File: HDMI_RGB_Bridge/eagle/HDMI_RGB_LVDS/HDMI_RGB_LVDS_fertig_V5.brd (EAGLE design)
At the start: 90 x 60 mm, 92 parts, among them CON1 KLDX-0202-A-LT, CON2 FCI-10029449-111RLF, CON3 XF2M-4015-1A, CON4 FCI-10033526-N3212LF, CON5 MOLEX-53261-0671, CON6 FI-X30SSLA-HF, IC2 WPMDL1300331BD, IC4 AT24C01C-SSHM-B, IC5 TFP401APZP, IC6 ATMEGA48A-AU, IC7 FT232RL, IC8 SN75LVDS83BDGGR, Q1 ATS073ASM-1, T1 IRF9530NSTRRPBF, T2 IRLML2502TRPBF

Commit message: schematic and layout adapted
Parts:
- removed C5: 10u, SchlegelAr_Master:C_POL_4X4MM
- removed LED4: (no value), SchlegelAr_Master:LED0402
- added LED1: (no value), SchlegelAr_Master:LED0402
- added R14: 22R, SchlegelAr_Master:R0402
- C16, C18, C20: value 0.1u -> 100n
- IC6: value ATMEGA48A-AU -> ATMEGA88PA
- R19: value 10k -> 5k
- T1: value IRF9530NSTRRPBF -> IRLML5203TRPBF; device SchlegelAr_Master:D2PAK -> SchlegelAr_Master:SOT23
- moved C1 49.1 mm to (43.2, 53.4)
- moved R25 35.1 mm to (63.4, 19.6), turned to 0 degrees
- moved R15 34.7 mm to (29.1, 22.6), turned to 90 degrees
- moved CON1 33.4 mm to (59.5, 32.4), turned to 180 degrees
- moved JP3 33.3 mm to (31.1, 23.1), turned to 180 degrees
- moved LED2 30.9 mm to (65.7, 21.2), turned to 0 degrees
- moved R27 30.6 mm to (63.4, 21.2), turned to 0 degrees
- moved T1 30.1 mm to (62.9, 39.8)
- moved R20 25.7 mm to (39.8, 55.6)
- moved T2 25.6 mm to (36.2, 54.6), turned to 0 degrees
- moved R1 24.9 mm to (66.0, 40.9), turned to 180 degrees
- moved IC2 20.8 mm to (59.6, 51.0)
- moved C2 17.6 mm to (66.0, 48.6), turned to 270 degrees
- moved JP2 10.1 mm to (58.0, 25.8), turned to 90 degrees
- moved R13 9.91 mm to (13.4, 5.00), flipped to the bottom
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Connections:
- new net N$1: IC6.13, R14.1
- net +12V: now also LED2.C, T1.2; no longer LED4.C, T1.3
- net +3V3: now also LED1.C; no longer LED2.C
- net AVR_PWM: now also R14.2; no longer IC6.13
- net N$2: now also T1.3; no longer T1.2
- net N$6: now also LED1.A; no longer LED2.A
- net N$8: now also LED2.A; no longer LED4.A
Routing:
- net +12V: track 135.6 -> 164.4 mm, vias 3 -> 12
- net RGB_DISP: track 50.7 -> 21.8 mm, vias 2 -> 0
- net N$37: track 36.5 -> 8.13 mm
- net RGB_PWM_EN: track 62.5 -> 39.7 mm, vias 2 -> 1
- net +3V3: track 77.5 -> 67.5 mm, vias 28 -> 36
- net N$2: track 14.9 -> 6.70 mm
- net +5V_USB: track 14.0 -> 20.8 mm
- net GND: track 146.6 -> 153.3 mm, vias 97 -> 103
- net HDMI_PIXS: track 13.6 -> 7.08 mm
- net N$1: track 0.00 -> 5.61 mm
- net LVDS_REVSCAN: track 40.9 -> 43.7 mm
- net AVR_PWM: track 5.25 -> 2.94 mm
- net INT_RGB_EVEN_B7: track 16.0 -> 17.5 mm
- net HDMI_OCK_INV: track 7.03 -> 5.66 mm
- net LVDS_PWM: track 26.2 -> 27.5 mm
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- added copper zone on layer 1, net +12V
- removed copper zone on layer 1, net +5V
- removed copper zone on layer 16, net +5V
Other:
- board size 90 x 60 mm -> 70 x 60 mm
- board text added: "02.04.2014"
- board text removed: "01.04.2014"
- board text removed: "TODO: vias verschieben, platine verkleiner, luftlinien killen"

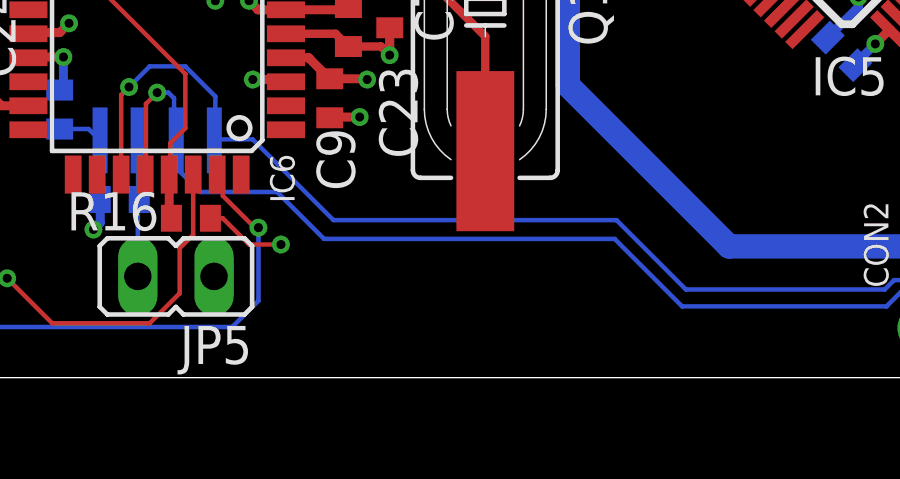
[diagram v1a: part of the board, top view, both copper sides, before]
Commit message: writing and reading to eeprom works - checksum needs to be fixed
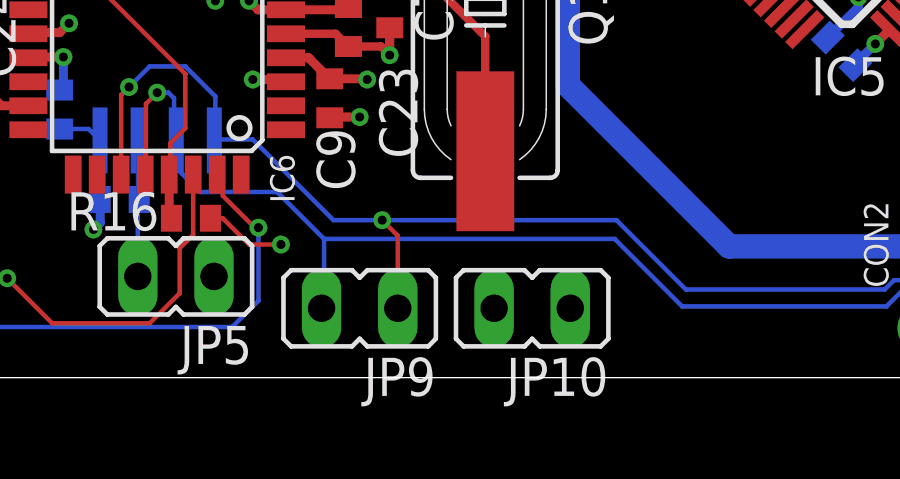
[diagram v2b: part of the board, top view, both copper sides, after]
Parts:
- added JP10, JP9: JUMPER2, SchlegelAr_Master:JUMPER2_THROUGHHOLE
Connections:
- net +5V: now also JP10.2
- net EDID_SCL: now also JP9.2
- net EDID_SDA: now also JP9.1
- net GND: now also JP10.1
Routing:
- net EDID_SDA: track 50.6 -> 53.8 mm, vias 2 -> 3
- net EDID_SCL: track 50.9 -> 53.3 mm
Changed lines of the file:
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@@
 <layers>
 <layer number="1" name="Top" color="4" fill="1" visible="yes" active="yes"/>
-<layer number="2" name="Route2" color="1" fill="3" visible="no" active="yes"/>
+<layer number="2" name="Route2" color="1" fill="3" visible="yes" active="yes"/>
 <layer number="3" name="Route3" color="4" fill="3" visible="no" active="no"/>
 <layer number="14" name="Route14" color="1" fill="6" visible="no" active="no"/>
-<layer number="15" name="Route15" color="4" fill="6" visible="no" active="yes"/>
+<layer number="15" name="Route15" color="4" fill="6" visible="yes" active="yes"/>
 <layer number="16" name="Bottom" color="1" fill="1" visible="yes" active="yes"/>
 <layer number="17" name="Pads" color="2" fill="1" visible="yes" active="yes"/>
@@
 <layer number="19" name="Unrouted" color="6" fill="1" visible="yes" active="yes"/>
 <layer number="20" name="Dimension" color="15" fill="1" visible="yes" active="yes"/>
-<layer number="21" name="tPlace" color="7" fill="1" visible="no" active="yes"/>
+<layer number="21" name="tPlace" color="7" fill="1" visible="yes" active="yes"/>
 <layer number="22" name="bPlace" color="7" fill="1" visible="no" active="yes"/>
-<layer number="23" name="tOrigins" color="15" fill="1" visible="no" active="yes"/>
+<layer number="23" name="tOrigins" color="15" fill="1" visible="yes" active="yes"/>
 <layer number="24" name="bOrigins" color="15" fill="1" visible="no" active="yes"/>
 <layer number="25" name="tNames" color="7" fill="1" visible="no" active="yes"/>
@@
 <attribute name="VALUE" x="24.865" y="13.7825" size="1.27" layer="27"/>
 </element>
+<element name="JP9" library="SchlegelAr_Master" package="JUMPER2_THROUGHHOLE" value="JUMPER2" x="27.5" y="2.3125" rot="R90"/>
+<element name="JP10" library="SchlegelAr_Master" package="JUMPER2_THROUGHHOLE" value="JUMPER2" x="33.25" y="2.3125" rot="R90"/>
 </elements>
 <signals>
@@
 <via x="28.1875" y="51.25" extent="1-16" drill="0.3"/>
 <via x="28.875" y="50.5625" extent="1-16" drill="0.3"/>
+<contactref element="JP10" pad="1"/>
 </signal>
 <signal name="+3V3">
@@
 <wire x1="14.0875" y1="5" x2="15" y2="5" width="0.3" layer="16"/>
 <via x="15" y="5" extent="1-16" drill="0.3"/>
+<contactref element="JP10" pad="2"/>
 </signal>
 <signal name="N$2">
@@
 <wire x1="54.8125" y1="3.375" x2="56.875" y2="3.375" width="0.15" layer="16"/>
 <wire x1="56.875" y1="4.6875" x2="56.875" y2="3.375" width="0.15" layer="1"/>
-<wire x1="26.625" y1="5.25" x2="36.0625" y2="5.25" width="0.15" layer="16"/>
+<wire x1="26.625" y1="5.25" x2="28.0625" y2="5.25" width="0.15" layer="16"/>
+<wire x1="28.25" y1="5.25" x2="36.0625" y2="5.25" width="0.15" layer="16"/>
 <wire x1="36.0625" y1="5.25" x2="38.375" y2="2.9375" width="0.15" layer="16"/>
 <contactref element="R28" pad="1"/>
 <wire x1="57.9125" y1="2.5" x2="57.75" y2="2.5" width="0.15" layer="16"/>
 <wire x1="57.75" y1="2.5" x2="56.875" y2="3.375" width="0.15" layer="16"/>
+<contactref element="JP9" pad="1"/>
+<wire x1="28.77" y1="2.3125" x2="28.77" y2="4.73" width="0.15" layer="1"/>
+<wire x1="28.77" y1="4.73" x2="28.25" y2="5.25" width="0.15" layer="1"/>
+<via x="28.25" y="5.25" extent="1-16" drill="0.3"/>
+<wire x1="28.25" y1="5.25" x2="28.0625" y2="5.25" width="0.15" layer="16"/>
 </signal>
 <signal name="EDID_SCL">
@@
 <wire x1="57.9125" y1="1.3125" x2="56.625" y2="1.3125" width="0.15" layer="16"/>
 <wire x1="56.625" y1="1.3125" x2="55.3125" y2="2.625" width="0.15" layer="16"/>
+<contactref element="JP9" pad="2"/>
+<wire x1="26.3125" y1="4.625" x2="26.3125" y2="2.395" width="0.15" layer="16"/>
+<wire x1="26.3125" y1="2.395" x2="26.23" y2="2.3125" width="0.15" layer="16"/>
 </signal>
 <signal name="N$18">
